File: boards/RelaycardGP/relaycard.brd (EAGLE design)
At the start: 101.6 x 74.9 mm, 34 parts, among them IC1 ULN2801A, K3 NA, K4 NA, K5 NA, K6 NA, K7 NA, X1 112404, X15 112404, X16 112404, X2 112404, X3 112404, X4 112404, X5 112404, X6 112404, X7 112404, X8 112404

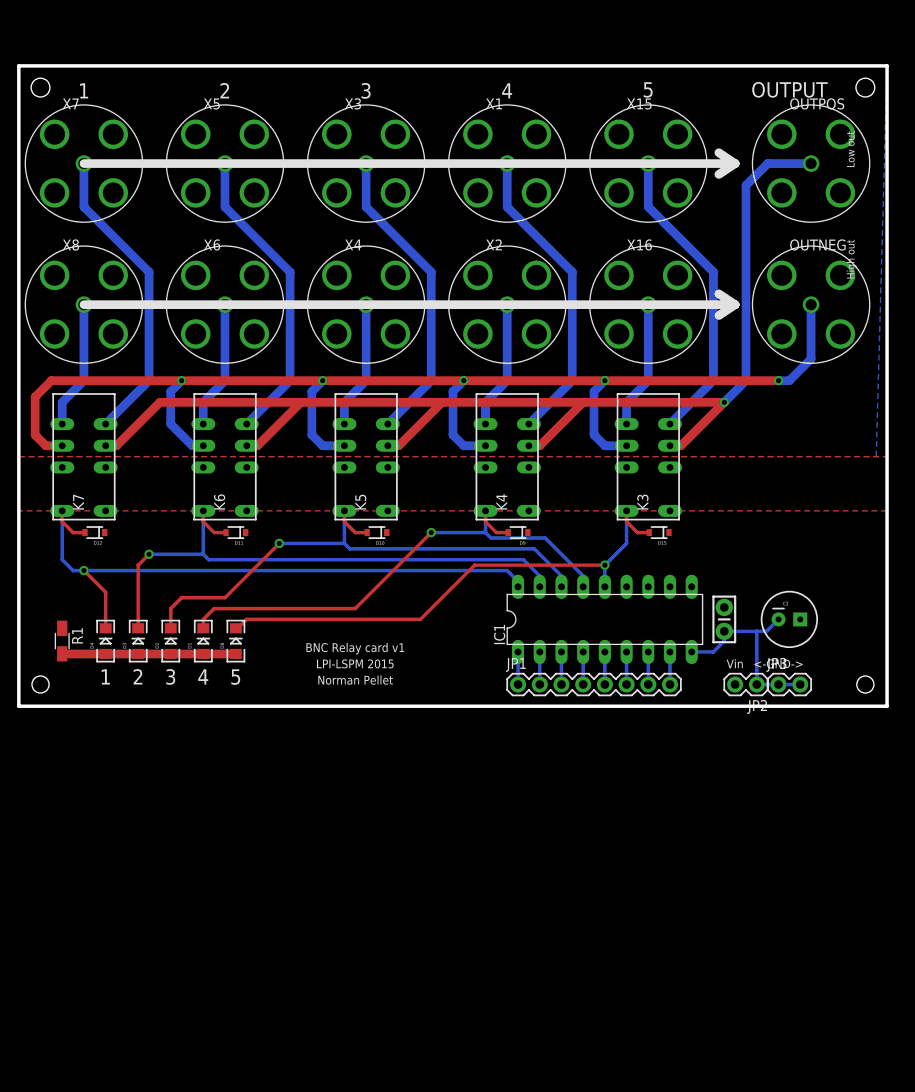
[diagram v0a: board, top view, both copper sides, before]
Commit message: Allow to remove methods
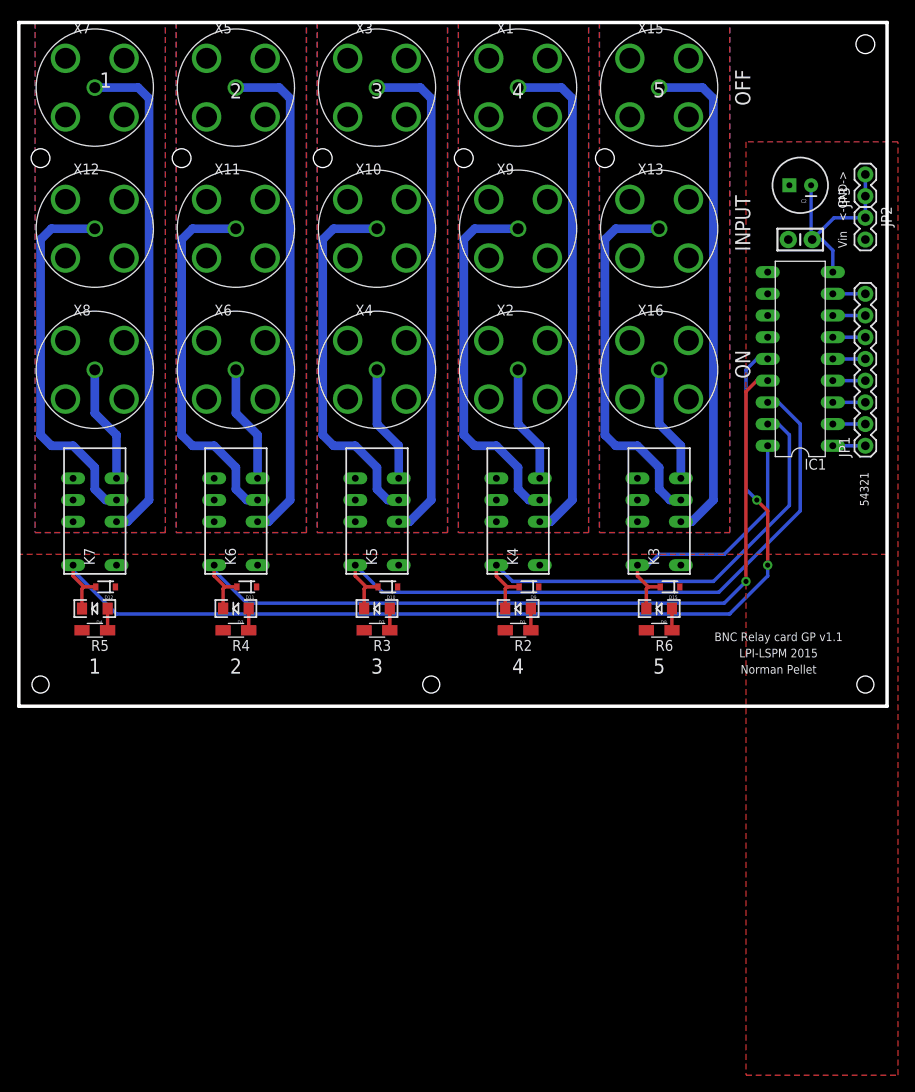
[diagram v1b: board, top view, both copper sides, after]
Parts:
- removed OUTNEG, OUTPOS: 112404, amphenol-112404_10:112404
- removed R1: (no value), resistor:R1206W
- added R2, R3, R4, R5, R6: (no value), resistor:R1206W
- added X10, X11, X12, X13, X9: 112404, amphenol-112404_10:112404
- moved JP3 58.0 mm to (99.1, 59.7), turned to 90 degrees
- moved JP2 56.1 mm to (99.1, 57.1), turned to 270 degrees
- moved C2 50.8 mm to (91.4, 61.0), turned to 180 degrees
- moved D8 49.7 mm to (74.9, 11.4), turned to 180 degrees
- moved JP1 49.3 mm to (99.1, 30.5), turned to 90 degrees
- moved C1 45.3 mm to (91.4, 54.6), turned to 180 degrees
- moved IC1 38.1 mm to (91.4, 40.6), turned to 90 degrees
- moved D1 37.0 mm to (58.4, 11.4), turned to 180 degrees
- moved D2 24.4 mm to (41.9, 11.4), turned to 180 degrees
- moved D3 12.0 mm to (25.4, 11.4), turned to 180 degrees
- moved X1 8.98 mm to (58.4, 72.4)
- moved X15 8.98 mm to (74.9, 72.4)
- moved X5 8.98 mm to (25.4, 72.4)
- moved X7 8.98 mm to (8.89, 72.4)
- moved X3 8.98 mm to (41.9, 72.4)
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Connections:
- removed net GND: OUTNEG.2, OUTNEG.3, OUTNEG.4, OUTNEG.5, OUTPOS.2, OUTPOS.3, OUTPOS.4, OUTPOS.5, X1.2, X1.3, X1.4, X1.5, X15.2, X15.3, X15.4, X15.5, X16.2, X16.3, X16.4, X16.5, X2.2, X2.3, X2.4, X2.5, X3.2, X3.3, X3.4, X3.5, X4.2, X4.3, X4.4, X4.5, X5.2, X5.3, X5.4, X5.5, X6.2, X6.3, X6.4, X6.5, X7.2, X7.3, X7.4, X7.5, X8.2, X8.3, X8.4, X8.5
- removed net N$24: K3.5, X15.1
- removed net N$25: K3.8, X16.1
- removed net OUTNEG: K3.9, K4.9, K5.9, K6.9, K7.9, OUTNEG.1
- removed net OUTPOS: K3.4, K4.4, K5.4, K6.4, K7.4, OUTPOS.1
- removed net RES: D1.A, D2.A, D3.A, D4.A, D8.A, R1.2
- new net A: D1.A, R2.1
- new net B: D2.A, R3.1
- new net C: D3.A, R4.1
- new net D: D4.A, R5.1
- new net E: D8.A, R6.1
- new net GND1: X1.2, X1.3, X1.4, X1.5, X2.2, X2.3, X2.4, X2.5, X9.2, X9.3, X9.4, X9.5
- new net GND3: X11.2, X11.3, X11.4, X11.5, X5.2, X5.3, X5.4, X5.5, X6.2, X6.3, X6.4, X6.5
- new net GND4: X12.2, X12.3, X12.4, X12.5, X7.2, X7.3, X7.4, X7.5, X8.2, X8.3, X8.4, X8.5
- new net GND5: X13.2, X13.3, X13.4, X13.5, X15.2, X15.3, X15.4, X15.5, X16.2, X16.3, X16.4, X16.5
- new net GND_V: C1.1, C2.2, IC1.9, JP2.1, JP3.1, JP3.2
- new net N$13: K5.4, X10.1
- new net N$15: K6.5, X6.1
- new net N$16: K6.4, X11.1
- new net N$17: K7.3, X7.1
- new net N$19: K7.5, X8.1
- new net N$20: K7.4, X12.1
- new net N$22: K3.5, X16.1
- net GND2: now also X10.2, X10.3, X10.4, X10.5, X3.2, X3.3, X3.4, X3.5, X4.2, X4.3, X4.4, X4.5; no longer C1.1, C2.2, IC1.9, JP2.1, JP3.1, JP3.2
- net N$1: now also X2.1; no longer X1.1
- net N$14: now also K6.3, X5.1; no longer K6.8, X6.1
- net N$21: now also K3.3, X15.1; no longer K7.5, X7.1
- net N$23: now also K3.4, X13.1; no longer K7.8, X8.1
- net N$3: now also K4.3, X1.1; no longer K4.8, X2.1
- net N$4: now also K4.4, X9.1; no longer K5.5, X3.1
- net N$5: now also K5.5; no longer K5.8
- net N$7: now also K5.3, X3.1; no longer K6.5, X5.1
- net RELAY1: now also D1.C, D9.A, IC1.17, K4.12; no longer D12.A, D4.C, IC1.18, K7.12
- net RELAY2: now also D10.A, D2.C, IC1.16, K5.12; no longer D11.A, D3.C, IC1.17, K6.12
- net RELAY3: now also D11.A, D3.C, IC1.15, K6.12; no longer D10.A, D2.C, IC1.16, K5.12
- net RELAY4: now also D12.A, D4.C, IC1.14, K7.12; no longer D1.C, D9.A, IC1.15, K4.12
- net RELAY5: now also IC1.18; no longer IC1.14
- net VCC: now also R2.2, R3.2, R4.2, R5.2, R6.2; no longer R1.1
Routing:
- net OUTNEG: track 151.2 -> 0.00 mm, vias 5 -> 0
- net OUTPOS: track 143.4 -> 0.00 mm, vias 1 -> 0
- net RELAY4: track 60.1 -> 121.2 mm, vias 1 -> 2
- net N$17: track 0.00 -> 58.7 mm
- net N$14: track 15.0 -> 58.7 mm
- net N$3: track 15.0 -> 58.7 mm
- net N$13: track 0.00 -> 43.3 mm
- net N$20: track 0.00 -> 43.3 mm
- net N$16: track 0.00 -> 43.3 mm
- net N$24: track 35.7 -> 0.00 mm
- net RELAY3: track 62.3 -> 97.9 mm
- net N$23: track 15.0 -> 43.3 mm
- net RELAY5: track 60.6 -> 32.6 mm, vias 1 -> 0
- net GND_V: track 0.00 -> 24.2 mm
- net GND2: track 23.7 -> 0.00 mm
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- added copper zone on layer 1, net GND1
- added copper zone on layer 16, net GND1
- added copper zone on layer 1, net GND2
- added copper zone on layer 16, net GND2
- added copper zone on layer 1, net GND3
- added copper zone on layer 16, net GND3
- added copper zone on layer 1, net GND4
- added copper zone on layer 16, net GND4
- added copper zone on layer 1, net GND5
- added copper zone on layer 16, net GND5
- removed copper zone on layer 1, net GND
- removed copper zone on layer 16, net GND
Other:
- board size 101.6 x 74.9 mm -> 101.6 x 80 mm
- board text added: "54321"
- board text added: "BNC Relay card GP v1.1"
- board text added: "INPUT"
- board text added: "OFF"
- board text added: "ON"
- board text removed: "BNC Relay card v1"
- board text removed: "High out"
- board text removed: "Low out"
- board text removed: "OUTPUT"
